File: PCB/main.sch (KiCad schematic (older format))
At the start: 41 parts, among them CON1 BARREL_JACK, P1 JUMPER_LEFT, P2 LEFT, P3 JUMPER_RIGHT, P4 RIGHT, SW1 SW_PUSH, SW2 SW_PUSH, SW3 SW_PUSH, U1 LM317T, U2 LM317T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

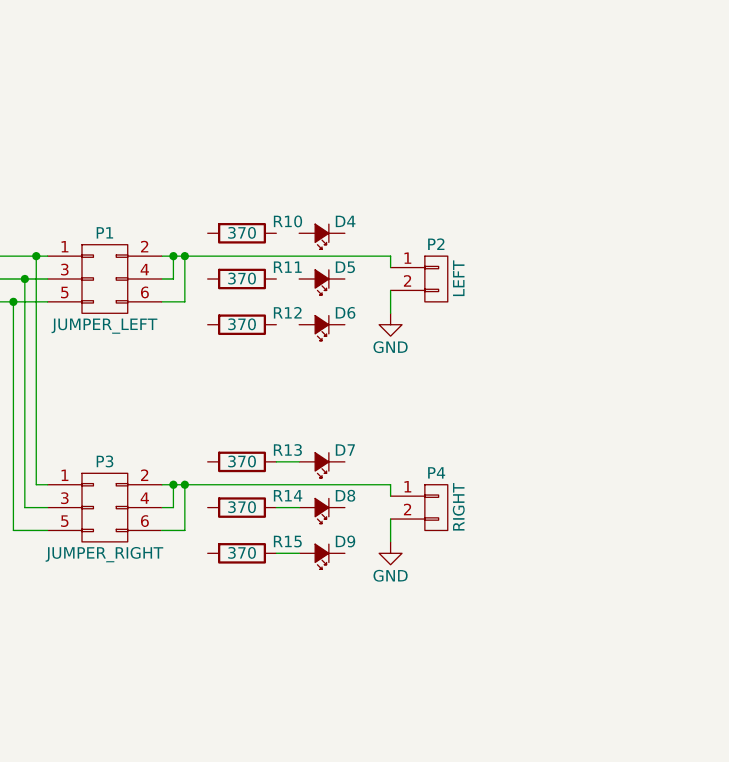
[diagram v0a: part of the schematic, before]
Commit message: led output circuit
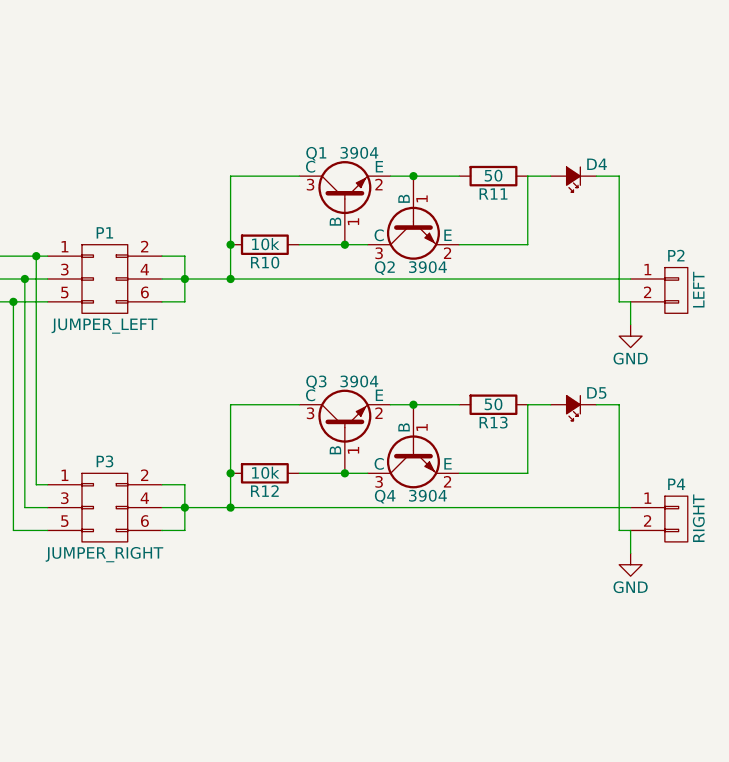
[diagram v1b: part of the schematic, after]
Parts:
- removed D4, D6, D8, D9: Led_Small, LEDs:LED-3MM, symbol Led_Small
- removed R14, R15: 370, Resistors_ThroughHole:Resistor_Horizontal_RM7mm, symbol R
- added Q1, Q2, Q3, Q4: 3904, TO_SOT_Packages_SMD:SOT-23, symbol MMBT3904
- R10, R12: value 370 -> 10k
- R11, R13: value 370 -> 50
- renumbered D7 to D4
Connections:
- net GND: now also D4.1 (K), D5.1 (K)
- net at P1.2 (P2), P1.4 (P4), P1.6 (P6)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: now also R10.2, Q1.3 (C)
- net at P3.2 (P2), P3.4 (P4), P3.6 (P6)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: now also R12.2, Q3.3 (C)
- net at D4.2 (A): now also R11.1, Q2.2 (E); no longer R13.1
- net at R13.2: now also Q3.2 (E), Q4.1 (B)
- net at R11.2: now also Q1.2 (E), Q2.1 (B)
- net at R10.1: now also Q1.1 (B), Q2.3 (C)
- net at R12.1: now also Q3.1 (B), Q4.3 (C)
- net at D5.2 (A): now also R13.1, Q4.2 (E)
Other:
- moved on the sheet: D4, P2, P4

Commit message: begin pcb layout
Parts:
- D1, D2, D3, D4, D5: footprint LEDs:LED-3MM -> LEDs:LED_0805
- R11, R13: value 50 -> 680
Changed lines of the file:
@@
 F 0 "D1" H 5450 2725 50  0000 L CNN
 F 1 "LED" H 5450 2500 50  0000 L CNN
-F 2 "LEDs:LED-3MM" V 5500 2600 50  0001 C CNN
+F 2 "LEDs:LED_0805" V 5500 2600 50  0001 C CNN
 F 3 "" V 5500 2600 50  0000 C CNN
 	1    5500 2600
@@
 F 0 "D2" H 5450 3725 50  0000 L CNN
 F 1 "LED" H 5450 3500 50  0000 L CNN
-F 2 "LEDs:LED-3MM" V 5500 3600 50  0001 C CNN
+F 2 "LEDs:LED_0805" V 5500 3600 50  0001 C CNN
 F 3 "" V 5500 3600 50  0000 C CNN
 	1    5500 3600
@@
 F 0 "D3" H 5450 4725 50  0000 L CNN
 F 1 "LED" H 5450 4500 50  0000 L CNN
-F 2 "LEDs:LED-3MM" V 5500 4600 50  0001 C CNN
+F 2 "LEDs:LED_0805" V 5500 4600 50  0001 C CNN
 F 3 "" V 5500 4600 50  0000 C CNN
 	1    5500 4600
@@
 F 0 "D4" H 8350 2400 50  0000 L CNN
 F 1 "Led_Small" H 8325 2350 50  0001 L CNN
-F 2 "LEDs:LED-3MM" V 8500 2450 50  0001 C CNN
+F 2 "LEDs:LED_0805" V 8500 2450 50  0001 C CNN
 F 3 "" V 8500 2450 50  0000 C CNN
 	1    8500 2450
@@
 P 8150 2450
 F 0 "R11" V 8230 2450 50  0000 C CNN
-F 1 "50" V 8150 2450 50  0000 C CNN
+F 1 "680" V 8150 2450 50  0000 C CNN
 F 2 "Resistors_ThroughHole:Resistor_Horizontal_RM7mm" V 8080 2450 50  0001 C CNN
 F 3 "" H 8150 2450 50  0000 C CNN
@@
 P 8150 3450
 F 0 "R13" V 8230 3450 50  0000 C CNN
-F 1 "50" V 8150 3450 50  0000 C CNN
+F 1 "680" V 8150 3450 50  0000 C CNN
 F 2 "Resistors_ThroughHole:Resistor_Horizontal_RM7mm" V 8080 3450 50  0001 C CNN
 F 3 "" H 8150 3450 50  0000 C CNN
@@
 F 0 "D5" H 8350 3400 50  0000 L CNN
 F 1 "Led_Small" H 8325 3350 50  0001 L CNN
-F 2 "LEDs:LED-3MM" V 8500 3450 50  0001 C CNN
+F 2 "LEDs:LED_0805" V 8500 3450 50  0001 C CNN
 F 3 "" V 8500 3450 50  0000 C CNN
 	1    8500 3450

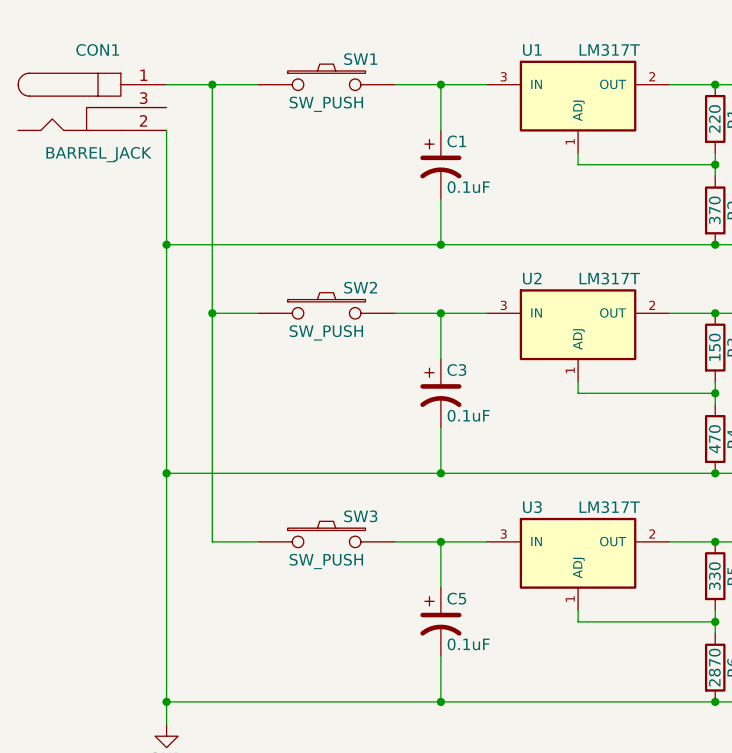
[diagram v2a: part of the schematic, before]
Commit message: real switches and oshpark test
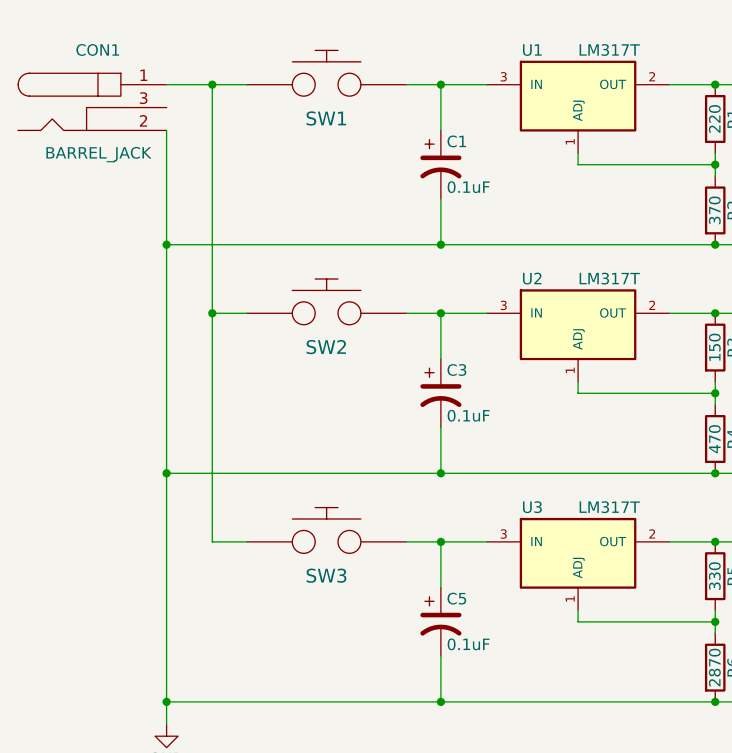
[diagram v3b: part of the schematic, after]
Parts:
- removed SW1, SW2, SW3: SW_PUSH, Buttons_Switches_ThroughHole:SW_PUSH-12mm, symbol SW_PUSH
- added SW1, SW2, SW3: 12x12_PUSHBUTTON_SPST, myparts:12x12_PUSHBUTTON_SPST, symbol 12x12_PUSHBUTTON_SPST
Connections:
- net at CON1.1: now also SW1.1, SW2.1, SW3.1
- net at C1.1, U1.3 (IN): now also SW1.2
- net at C3.1, U2.3 (IN): now also SW2.2
- net at C5.1, U3.3 (IN): now also SW3.2
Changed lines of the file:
@@
 EESchema Schematic File Version 2
+LIBS:myparts
 LIBS:power
 LIBS:device
@@
 $EndComp
 $Comp
-L SW_PUSH SW1
-U 1 1 57084324
-P 3000 2050
-F 0 "SW1" H 3150 2160 50  0000 C CNN
-F 1 "SW_PUSH" H 3000 1970 50  0000 C CNN
-F 2 "Buttons_Switches_ThroughHole:SW_PUSH-12mm" H 3000 2050 50  0001 C CNN
-F 3 "" H 3000 2050 50  0000 C CNN
-	1    3000 2050
-	1    0    0    -1
-$EndComp
-$Comp
-L SW_PUSH SW2
-U 1 1 570843B1
-P 3000 3050
-F 0 "SW2" H 3150 3160 50  0000 C CNN
-F 1 "SW_PUSH" H 3000 2970 50  0000 C CNN
-F 2 "Buttons_Switches_ThroughHole:SW_PUSH-12mm" H 3000 3050 50  0001 C CNN
-F 3 "" H 3000 3050 50  0000 C CNN
-	1    3000 3050
-	1    0    0    -1
-$EndComp
-$Comp
-L SW_PUSH SW3
-U 1 1 570843E4
-P 3000 4050
-F 0 "SW3" H 3150 4160 50  0000 C CNN
-F 1 "SW_PUSH" H 3000 3970 50  0000 C CNN
-F 2 "Buttons_Switches_ThroughHole:SW_PUSH-12mm" H 3000 4050 50  0001 C CNN
-F 3 "" H 3000 4050 50  0000 C CNN
-	1    3000 4050
-	1    0    0    -1
-$EndComp
-$Comp
 L R R7
 U 1 1 57084419
@@
 $EndComp
 Wire Wire Line
-	2300 2050 2700 2050
-Wire Wire Line
-	3300 2050 3700 2050
-Wire Wire Line
-	3300 3050 3700 3050
-Wire Wire Line
-	2700 3050 2500 3050
-Wire Wire Line
 	2500 2050 2500 4050
 Connection ~ 2500 2050
-Wire Wire Line
-	2500 4050 2700 4050
 Connection ~ 2500 3050
-Wire Wire Line
-	3300 4050 3700 4050
 Wire Wire Line
 	4700 2350 4700 2450
@@
 Wire Wire Line
 	8700 3450 8600 3450
+$Comp
+L 12x12_PUSHBUTTON_SPST SW1
+U 1 1 5714D48E
+P 3000 2000
+F 0 "SW1" H 3000 1800 60  0000 C CNN
+F 1 "12x12_PUSHBUTTON_SPST" H 3000 2200 60  0001 C CNN
+F 2 "myparts:12x12_PUSHBUTTON_SPST" H 3000 2000 60  0001 C CNN
+F 3 "" H 3000 2000 60  0000 C CNN
+	1    3000 2000
+	1    0    0    -1
+$EndComp
+Wire Wire Line
+	2300 2050 2650 2050
+Wire Wire Line
+	3350 2050 3700 2050
+$Comp
+L 12x12_PUSHBUTTON_SPST SW2
+U 1 1 5714F8A0
+P 3000 3000
+F 0 "SW2" H 3000 2800 60  0000 C CNN
+F 1 "12x12_PUSHBUTTON_SPST" H 3000 3200 60  0001 C CNN
+F 2 "myparts:12x12_PUSHBUTTON_SPST" H 3000 3000 60  0001 C CNN
+F 3 "" H 3000 3000 60  0000 C CNN
+	1    3000 3000
+	1    0    0    -1
+$EndComp
+$Comp
+L 12x12_PUSHBUTTON_SPST SW3
+U 1 1 57150C98
+P 3000 4000
+F 0 "SW3" H 3000 3800 60  0000 C CNN
+F 1 "12x12_PUSHBUTTON_SPST" H 3000 4200 60  0001 C CNN
+F 2 "myparts:12x12_PUSHBUTTON_SPST" H 3000 4000 60  0001 C CNN
+F 3 "" H 3000 4000 60  0000 C CNN
+	1    3000 4000
+	1    0    0    -1
+$EndComp
+Wire Wire Line
+	3700 4050 3350 4050
+Wire Wire Line
+	2500 4050 2650 4050
+Wire Wire Line
+	3700 3050 3350 3050
+Wire Wire Line
+	2650 3050 2500 3050
 $EndSCHEMATC

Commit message: smaller pcb
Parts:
- C2, C4, C6: footprint Capacitors_ThroughHole:C_Radial_D5_L11_P2 -> Capacitors_ThroughHole:C_Radial_D6.3_L11.2_P2.5
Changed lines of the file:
@@
 F 0 "C2" H 5075 2500 50  0000 L CNN
 F 1 "220uF" H 5075 2300 50  0000 L CNN
-F 2 "Capacitors_ThroughHole:C_Radial_D5_L11_P2" H 5050 2400 50  0001 C CNN
+F 2 "Capacitors_ThroughHole:C_Radial_D6.3_L11.2_P2.5" H 5050 2400 50  0001 C CNN
 F 3 "" H 5050 2400 50  0000 C CNN
 	1    5050 2400
@@
 F 0 "C4" H 5075 3500 50  0000 L CNN
 F 1 "220uF" H 5075 3300 50  0000 L CNN
-F 2 "Capacitors_ThroughHole:C_Radial_D5_L11_P2" H 5050 3400 50  0001 C CNN
+F 2 "Capacitors_ThroughHole:C_Radial_D6.3_L11.2_P2.5" H 5050 3400 50  0001 C CNN
 F 3 "" H 5050 3400 50  0000 C CNN
 	1    5050 3400
@@
 F 0 "C6" H 5075 4500 50  0000 L CNN
 F 1 "220uF" H 5075 4300 50  0000 L CNN
-F 2 "Capacitors_ThroughHole:C_Radial_D5_L11_P2" H 5050 4400 50  0001 C CNN
+F 2 "Capacitors_ThroughHole:C_Radial_D6.3_L11.2_P2.5" H 5050 4400 50  0001 C CNN
 F 3 "" H 5050 4400 50  0000 C CNN
 	1    5050 4400

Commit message: fat holes for barrel jack
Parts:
- CON1: footprint Connect:BARREL_JACK -> mods:BARREL_JACK2
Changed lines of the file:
@@
 F 0 "CON1" H 2000 2400 50  0000 C CNN
 F 1 "BARREL_JACK" H 2000 1950 50  0000 C CNN
-F 2 "Connect:BARREL_JACK" H 2000 2150 50  0001 C CNN
+F 2 "mods:BARREL_JACK2" H 2000 2150 50  0001 C CNN
 F 3 "" H 2000 2150 50  0000 C CNN
 	1    2000 2150
